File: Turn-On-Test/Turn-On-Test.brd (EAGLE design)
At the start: 13.1 x 17.8 mm, 8 parts

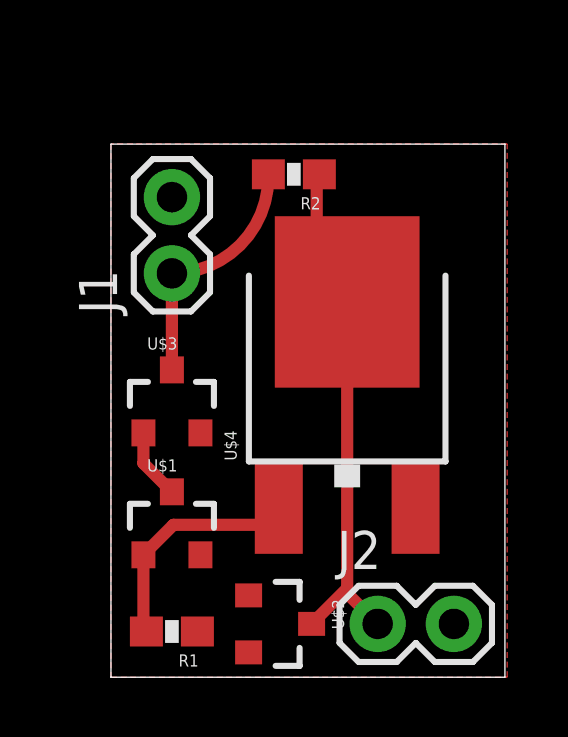
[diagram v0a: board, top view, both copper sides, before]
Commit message: finalized back silk
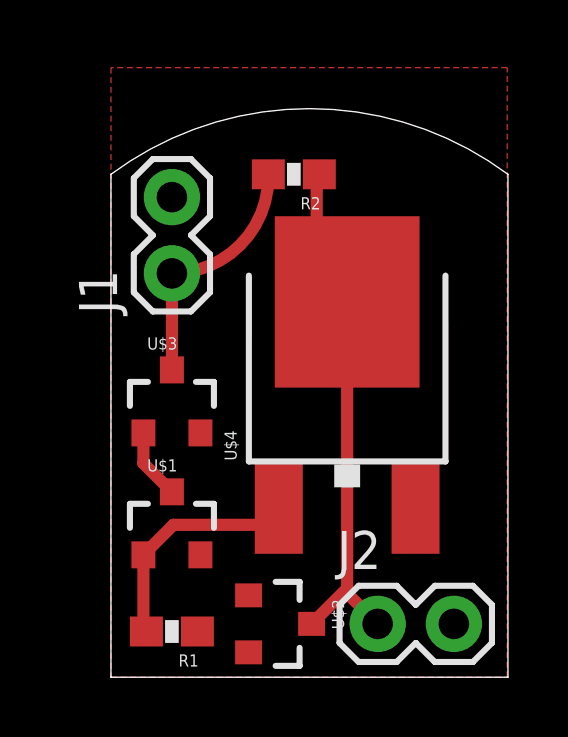
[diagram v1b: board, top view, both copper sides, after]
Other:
- board size 13.1 x 17.8 mm -> 13.2 x 19 mm
- board text added: "RHE"
- board text added: "ramp up trigger test board"

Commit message: created CAM job
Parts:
- moved J1 1.02 mm to (2.03, 12.4)
- moved R2 0.25 mm to (6.10, 16.5)
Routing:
- added copper zone on layer 16, net GND
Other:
- board size 13.2 x 19 mm -> 13.2 x 18.2 mm
- board text added: "H"
- board text added: "R E"
- board text added: "VIN GND"
- board text added: "VOUT GND"
- board text removed: "RHE"
